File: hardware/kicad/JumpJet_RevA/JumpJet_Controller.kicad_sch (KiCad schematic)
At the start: 4 parts, among them J5 SERVICE_HEADER, U2 ESP32-S3 SUPERMINI

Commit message: hardware: replace fan block with four-wire interface
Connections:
- net FAN_PWM renamed LEGACY_FAN_PWM_NC
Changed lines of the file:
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@@
     (effects (font (size 0.85 0.85)) (justify left bottom))
   )
-  (global_label "FAN_PWM" (shape bidirectional) (at 96.52 76.2 0) (fields_autoplaced)
+  (global_label "LEGACY_FAN_PWM_NC" (shape bidirectional) (at 96.52 76.2 0) (fields_autoplaced)
     (effects (font (size 0.85 0.85)) (justify left bottom))
   )

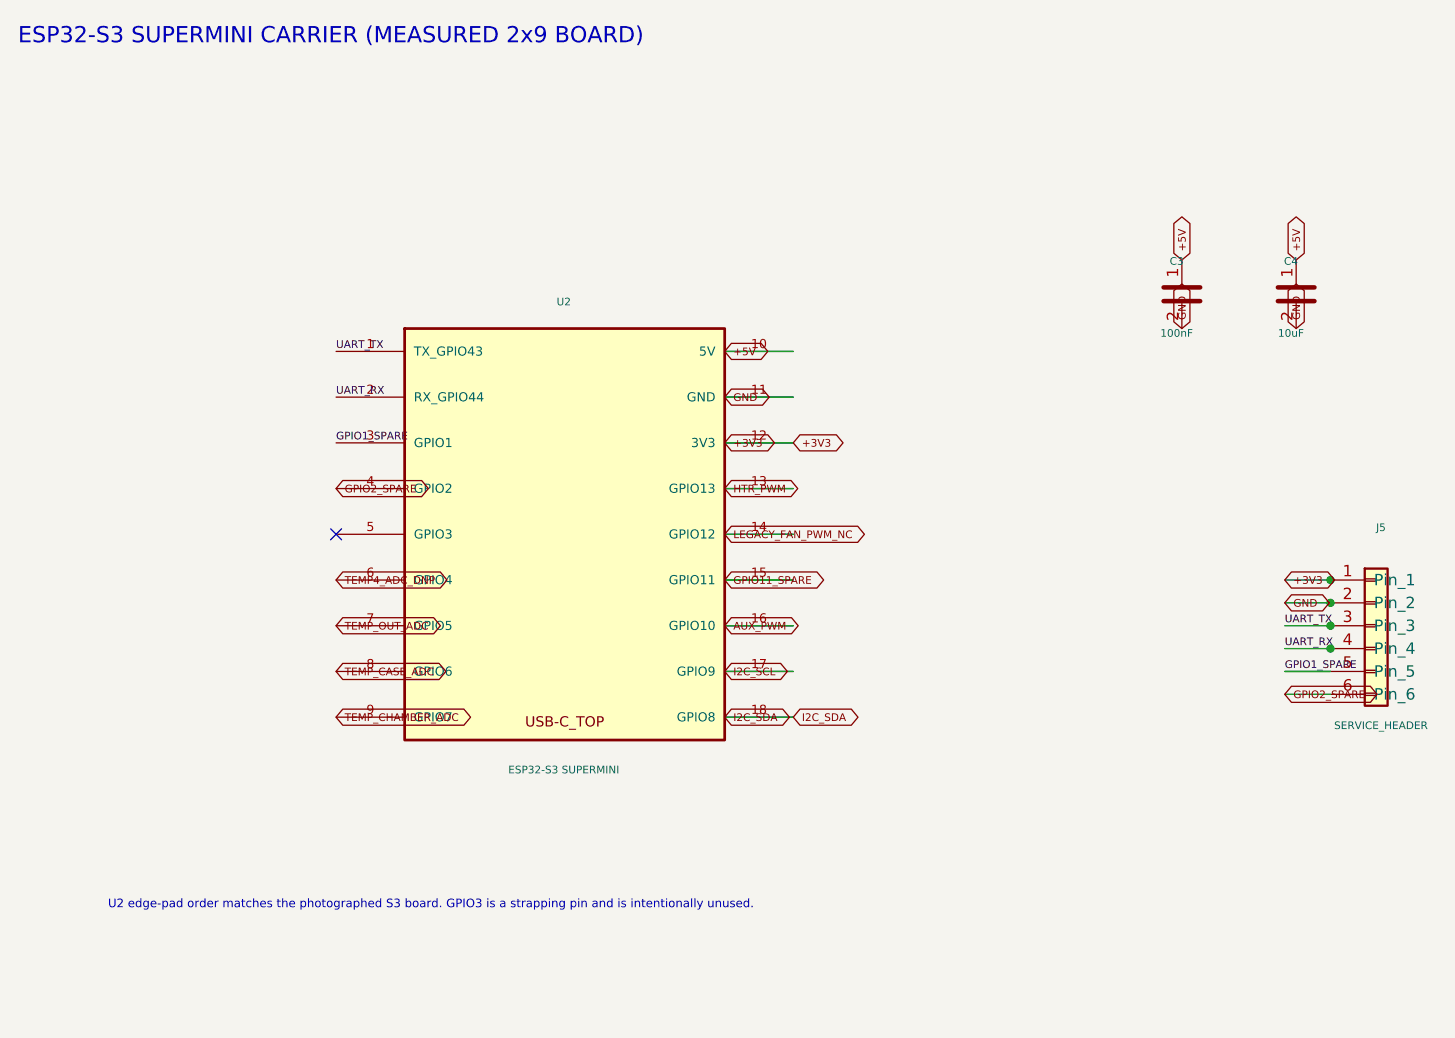
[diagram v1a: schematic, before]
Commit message: hardware: separate gate power and default-disable heater driver
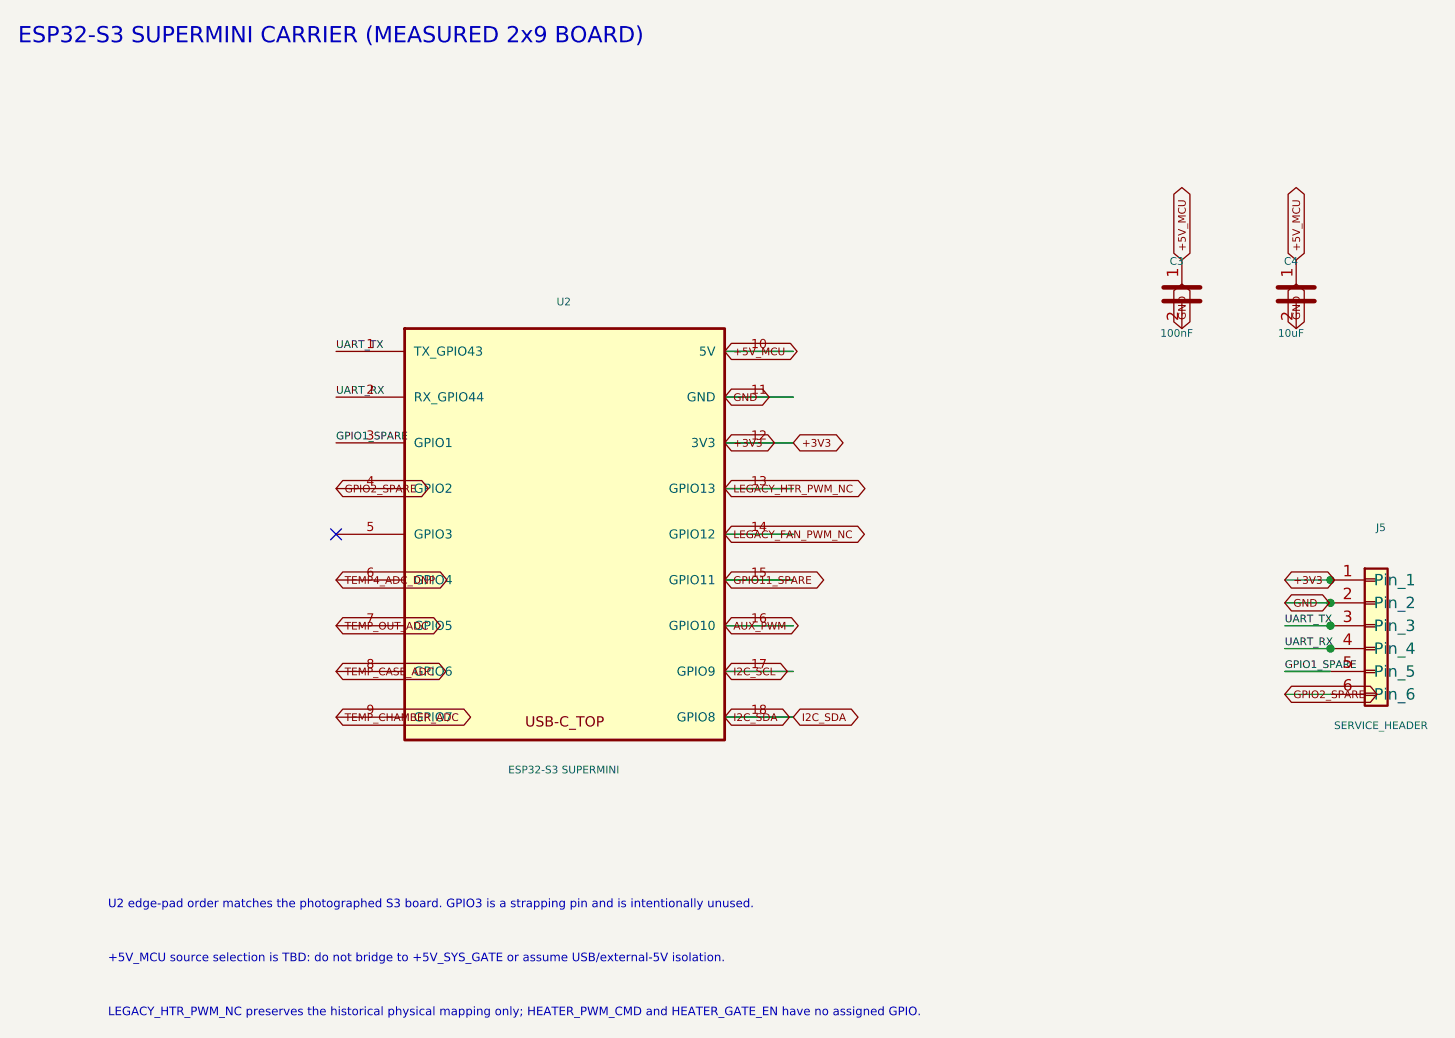
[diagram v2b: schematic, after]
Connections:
- net +5V renamed +5V_MCU
- net HTR_PWM renamed LEGACY_HTR_PWM_NC
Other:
- note added: "+5V_MCU source selection is TBD: do not bridge to +5V_SYS_GATE or assume USB/external-5V isolation."
- note added: "LEGACY_HTR_PWM_NC preserves the historical physical mapping only; HEATER_PWM_CMD and HEATER_GATE_EN have no assigned GPIO."
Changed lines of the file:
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@@
+    (effects (font (size 0.95 0.95) (thickness 0.120)) (justify left bottom))
+  )
+  (text "+5V_MCU source selection is TBD: do not bridge to +5V_SYS_GATE or assume USB/external-5V isolation."
+    (at 28.00 124.00 0)
+    (effects (font (size 0.95 0.95) (thickness 0.120)) (justify left bottom))
+  )
+  (text "LEGACY_HTR_PWM_NC preserves the historical physical mapping only; HEATER_PWM_CMD and HEATER_GATE_EN have no assigned GPIO."
+    (at 28.00 130.00 0)
     (effects (font (size 0.95 0.95) (thickness 0.120)) (justify left bottom))
   )
@@
     (effects (font (size 0.85 0.85)) (justify left bottom))
   )
-  (global_label "+5V" (shape bidirectional) (at 96.52 55.88 0) (fields_autoplaced)
+  (global_label "+5V_MCU" (shape bidirectional) (at 96.52 55.88 0) (fields_autoplaced)
     (effects (font (size 0.85 0.85)) (justify left bottom))
   )
@@
     (effects (font (size 0.85 0.85)) (justify left bottom))
   )
-  (global_label "HTR_PWM" (shape bidirectional) (at 96.52 71.12 0) (fields_autoplaced)
+  (global_label "LEGACY_HTR_PWM_NC" (shape bidirectional) (at 96.52 71.12 0) (fields_autoplaced)
     (effects (font (size 0.85 0.85)) (justify left bottom))
   )
@@
     (effects (font (size 0.85 0.85)) (justify left bottom))
   )
-  (global_label "+5V" (shape bidirectional) (at 160.02 45.72 90) (fields_autoplaced)
+  (global_label "+5V_MCU" (shape bidirectional) (at 160.02 45.72 90) (fields_autoplaced)
     (effects (font (size 0.85 0.85)) (justify left bottom))
   )
@@
     (effects (font (size 0.85 0.85)) (justify left bottom))
   )
-  (global_label "+5V" (shape bidirectional) (at 147.32 45.72 90) (fields_autoplaced)
+  (global_label "+5V_MCU" (shape bidirectional) (at 147.32 45.72 90) (fields_autoplaced)
     (effects (font (size 0.85 0.85)) (justify left bottom))
   )

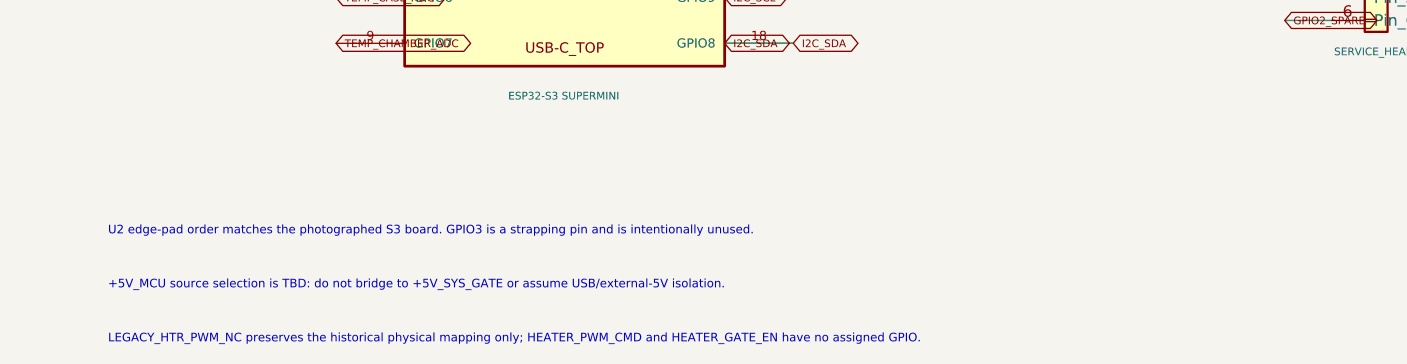
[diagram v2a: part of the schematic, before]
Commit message: hardware: require physical MCU service disconnect
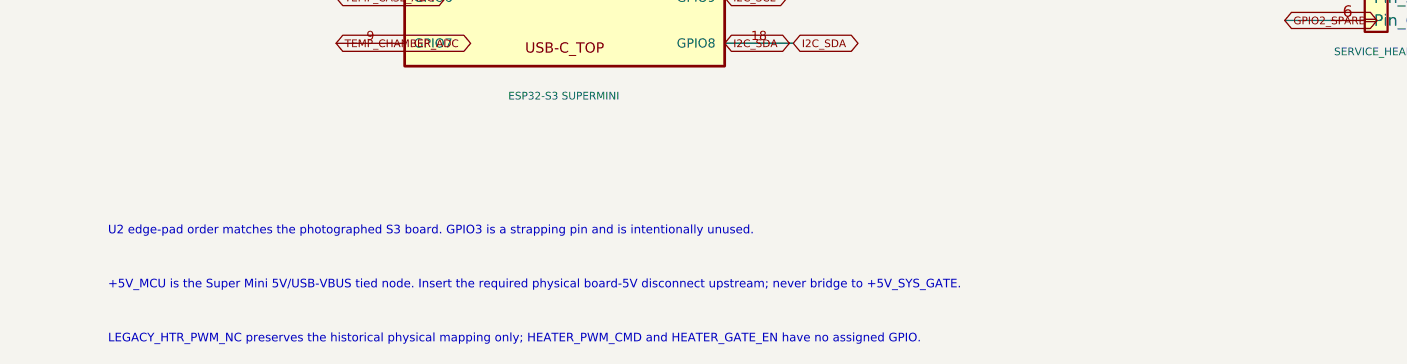
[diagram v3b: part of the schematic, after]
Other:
- note added: "+5V_MCU is the Super Mini 5V/USB-VBUS tied node. Insert the required physical board-5V disconnect upstream; never bridge to +5V_SYS_GATE."
- note removed: "+5V_MCU source selection is TBD: do not bridge to +5V_SYS_GATE or assume USB/external-5V isolation."
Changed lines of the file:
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@@
     (effects (font (size 0.95 0.95) (thickness 0.120)) (justify left bottom))
   )
-  (text "+5V_MCU source selection is TBD: do not bridge to +5V_SYS_GATE or assume USB/external-5V isolation."
+  (text "+5V_MCU is the Super Mini 5V/USB-VBUS tied node. Insert the required physical board-5V disconnect upstream; never bridge to +5V_SYS_GATE."
     (at 28.00 124.00 0)
     (effects (font (size 0.95 0.95) (thickness 0.120)) (justify left bottom))

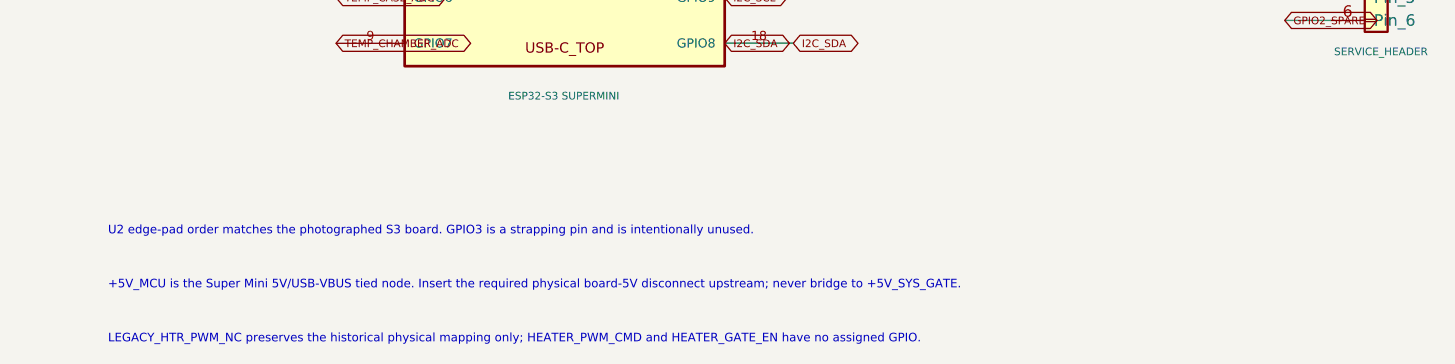
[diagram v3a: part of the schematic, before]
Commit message: hardware: implement MCU power isolation and service disconnect
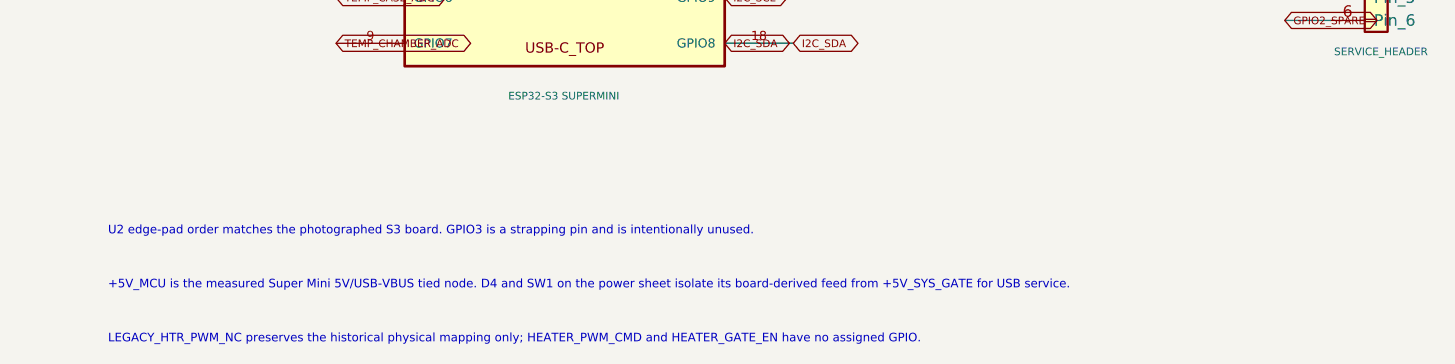
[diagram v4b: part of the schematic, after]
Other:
- note added: "+5V_MCU is the measured Super Mini 5V/USB-VBUS tied node. D4 and SW1 on the power sheet isolate its board-derived feed from +5V_SYS_GATE for USB service."
- note removed: "+5V_MCU is the Super Mini 5V/USB-VBUS tied node. Insert the required physical board-5V disconnect upstream; never bridge to +5V_SYS_GATE."
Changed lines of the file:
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@@
     (effects (font (size 0.95 0.95) (thickness 0.120)) (justify left bottom))
   )
-  (text "+5V_MCU is the Super Mini 5V/USB-VBUS tied node. Insert the required physical board-5V disconnect upstream; never bridge to +5V_SYS_GATE."
+  (text "+5V_MCU is the measured Super Mini 5V/USB-VBUS tied node. D4 and SW1 on the power sheet isolate its board-derived feed from +5V_SYS_GATE for USB service."
     (at 28.00 124.00 0)
     (effects (font (size 0.95 0.95) (thickness 0.120)) (justify left bottom))

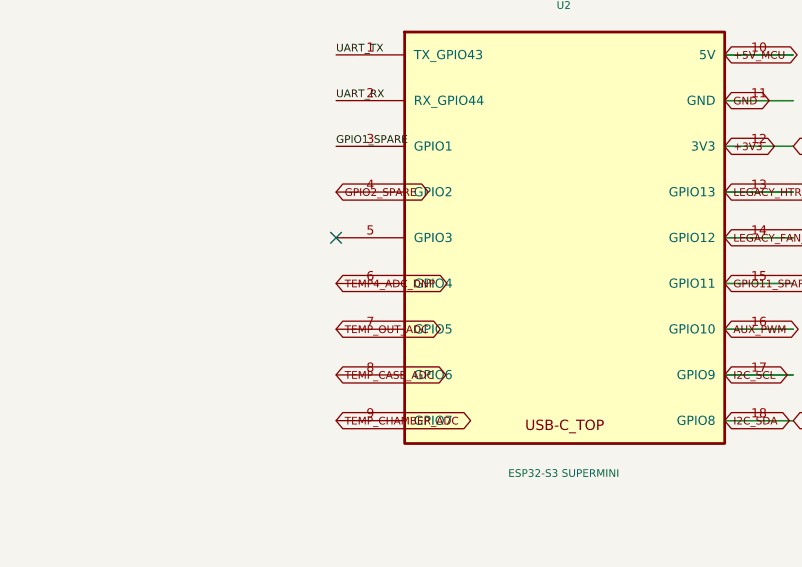
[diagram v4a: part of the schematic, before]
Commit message: hardware: add onboard PCB thermistor channel
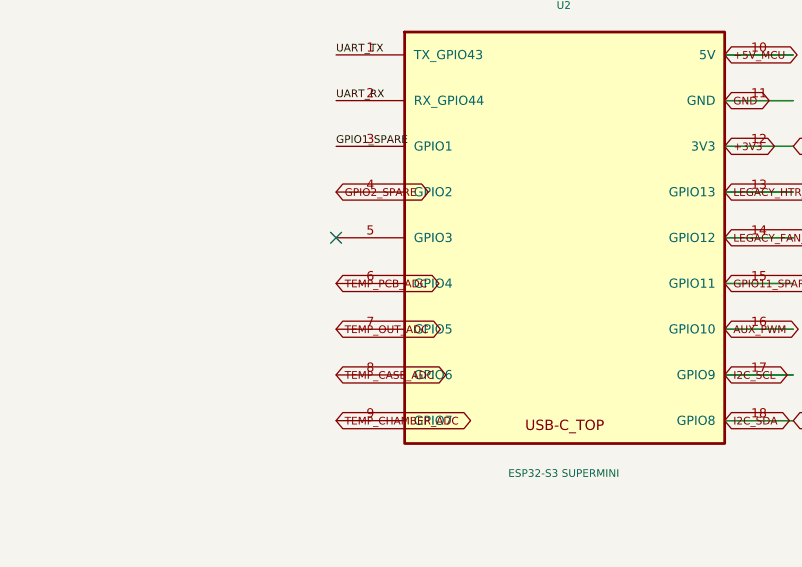
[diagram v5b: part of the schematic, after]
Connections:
- net TEMP4_ADC_DNP renamed TEMP_PCB_ADC
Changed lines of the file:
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@@
     (effects (font (size 0.85 0.85)) (justify left bottom))
   )
-  (global_label "TEMP4_ADC_DNP" (shape bidirectional) (at 53.34 81.28 0) (fields_autoplaced)
+  (global_label "TEMP_PCB_ADC" (shape bidirectional) (at 53.34 81.28 0) (fields_autoplaced)
     (effects (font (size 0.85 0.85)) (justify left bottom))
   )
